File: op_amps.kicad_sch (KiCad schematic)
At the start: 44 parts, among them U10 ${SIM.PARAMS}, U11 ${SIM.PARAMS}, U12 ${SIM.PARAMS}, U13 ${SIM.PARAMS}, U14 ${SIM.PARAMS}, U15 ${SIM.PARAMS}, U16 ${SIM.PARAMS}, U17 ${SIM.PARAMS}, U18 ${SIM.PARAMS}, U19 ${SIM.PARAMS}, U20 ${SIM.PARAMS}, U21 ${SIM.PARAMS}, U22 ${SIM.PARAMS}, U23 ${SIM.PARAMS}, U8 ${SIM.PARAMS}, U9 ${SIM.PARAMS}

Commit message: Updated: crossbar
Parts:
- C1, C2, C3, C4: footprint Capacitor_SMD:C_1206_3216Metric_Pad1.33x1.80mm_HandSolder -> Capacitor_SMD:C_1206_3216Metric
- R15, R16, R17, R18, R19, R20, R21, R22, R23, R24, R25, R26, R27, R28, R29, R30, R31, R32, R33, R34, R44, R45, R46, R47: footprint Resistor_SMD:R_1206_3216Metric_Pad1.30x1.75mm_HandSolder -> Resistor_SMD:R_1206_3216Metric
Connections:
- net VCC renamed VDD

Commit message: Updated: crossbar error
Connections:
- net z1*: no longer R22.1, R27.1, R32.1, U12.4 (-), U16.4 (-), U20.4 (-)
- new net z2*: R22.1, U12.4 (-)
- new net z3*: R27.1, U16.4 (-)
- new net z4*: R32.1, U20.4 (-)
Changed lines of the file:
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@@
 		)
 	)
-	(global_label "z1*"
+	(global_label "z2*"
 		(shape input)
 		(at 43.18 100.33 180)
@@
 		)
 	)
-	(global_label "z1*"
+	(global_label "z3*"
 		(shape input)
 		(at 43.18 148.59 180)
@@
 		)
 	)
-	(global_label "z1*"
+	(global_label "z4*"
 		(shape input)
 		(at 43.18 195.58 180)

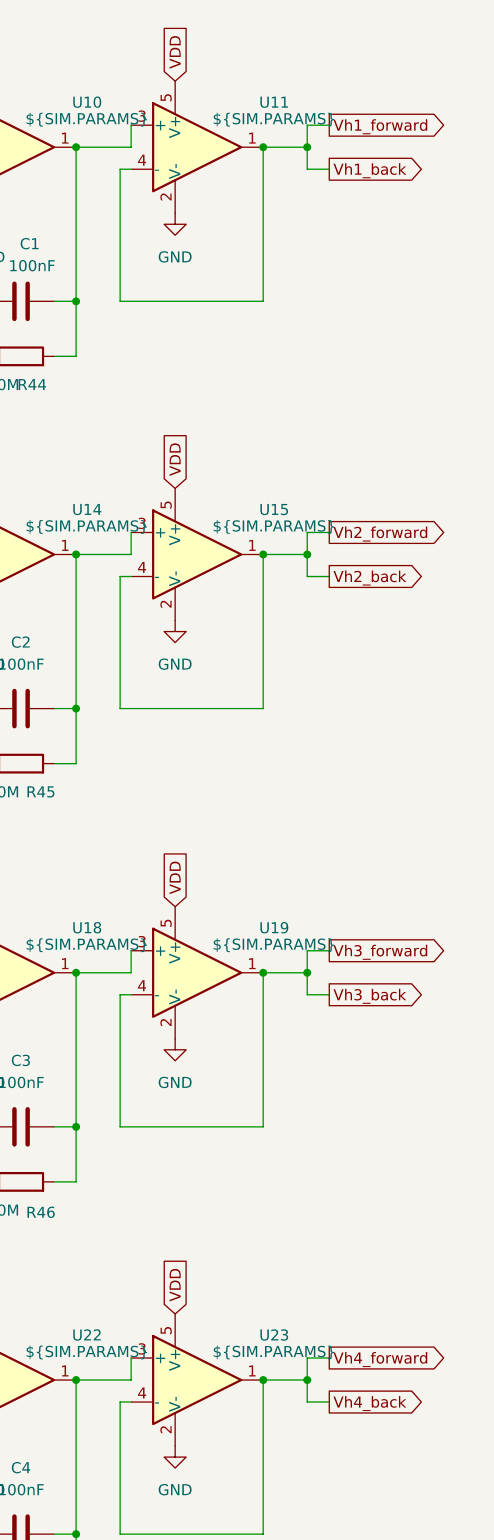
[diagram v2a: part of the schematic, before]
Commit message: Fixed: v closed loop
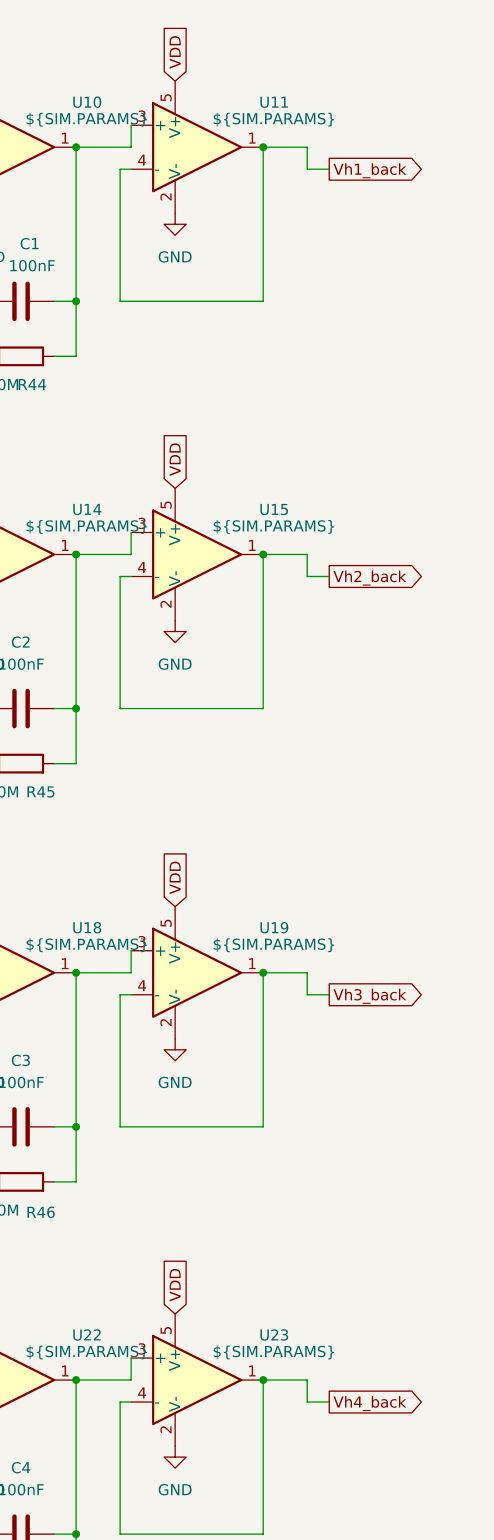
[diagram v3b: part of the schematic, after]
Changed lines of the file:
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@@
 	(paper "A4" portrait)
 	(junction
-		(at 153.67 148.59)
-		(diameter 0)
-		(color 0 0 0 0)
-	)
-	(junction
 		(at 127 166.37)
 		(diameter 0)
@@
 	)
 	(junction
-		(at 153.67 100.33)
-		(diameter 0)
-		(color 0 0 0 0)
-	)
-	(junction
 		(at 97.79 53.34)
 		(diameter 0)
@@
 	)
 	(junction
-		(at 153.67 53.34)
-		(diameter 0)
-		(color 0 0 0 0)
-	)
-	(junction
 		(at 49.53 151.13)
 		(diameter 0)
@@
 	)
 	(junction
-		(at 153.67 195.58)
-		(diameter 0)
-		(color 0 0 0 0)
-	)
-	(junction
 		(at 127 100.33)
 		(diameter 0)
@@
 	(wire
 		(pts
-			(xy 153.67 50.8) (xy 156.21 50.8)
-		)
-		(stroke
-			(width 0)
-			(type default)
-		)
-	)
-	(wire
-		(pts
 			(xy 132.08 151.13) (xy 133.35 151.13)
 		)
@@
 	(wire
 		(pts
-			(xy 153.67 146.05) (xy 153.67 148.59)
-		)
-		(stroke
-			(width 0)
-			(type default)
-		)
-	)
-	(wire
-		(pts
 			(xy 132.08 198.12) (xy 132.08 213.36)
 		)
@@
 	(wire
 		(pts
-			(xy 153.67 193.04) (xy 156.21 193.04)
-		)
-		(stroke
-			(width 0)
-			(type default)
-		)
-	)
-	(wire
-		(pts
 			(xy 49.53 55.88) (xy 49.53 71.12)
 		)
@@
 	(wire
 		(pts
-			(xy 153.67 97.79) (xy 156.21 97.79)
-		)
-		(stroke
-			(width 0)
-			(type default)
-		)
-	)
-	(wire
-		(pts
 			(xy 148.59 148.59) (xy 153.67 148.59)
 		)
@@
 	(wire
 		(pts
-			(xy 153.67 50.8) (xy 153.67 53.34)
-		)
-		(stroke
-			(width 0)
-			(type default)
-		)
-	)
-	(wire
-		(pts
 			(xy 153.67 100.33) (xy 153.67 102.87)
 		)
@@
 	(wire
 		(pts
-			(xy 153.67 146.05) (xy 156.21 146.05)
-		)
-		(stroke
-			(width 0)
-			(type default)
-		)
-	)
-	(wire
-		(pts
 			(xy 148.59 71.12) (xy 132.08 71.12)
 		)
@@
 	(wire
 		(pts
-			(xy 153.67 97.79) (xy 153.67 100.33)
-		)
-		(stroke
-			(width 0)
-			(type default)
-		)
-	)
-	(wire
-		(pts
 			(xy 148.59 100.33) (xy 153.67 100.33)
 		)
@@
 		(pts
 			(xy 111.76 213.36) (xy 116.84 213.36)
-		)
-		(stroke
-			(width 0)
-			(type default)
-		)
-	)
-	(wire
-		(pts
-			(xy 153.67 193.04) (xy 153.67 195.58)
 		)
 		(stroke
@@
 		)
 	)
-	(global_label "Vh4_forward"
-		(shape output)
-		(at 156.21 193.04 0)
-		(fields_autoplaced yes)
-		(effects
-			(font
-				(size 1.27 1.27)
-			)
-			(justify left)
-		)
-		(property "Intersheetrefs" "${INTERSHEET_REFS}"
-			(at 170.6855 193.04 0)
-			(effects
-				(font
-					(size 1.27 1.27)
-				)
-				(justify left)
-				(hide yes)
-			)
-		)
-	)
 	(global_label "VREF"
 		(shape input)
@@
 		)
 	)
-	(global_label "Vh3_forward"
-		(shape output)
-		(at 156.21 146.05 0)
-		(fields_autoplaced yes)
-		(effects
-			(font
-				(size 1.27 1.27)
-			)
-			(justify left)
-		)
-		(property "Intersheetrefs" "${INTERSHEET_REFS}"
-			(at 170.6855 146.05 0)
-			(effects
-				(font
-					(size 1.27 1.27)
-				)
-				(justify left)
-				(hide yes)
-			)
-		)
-	)
 	(global_label "z4*"
 		(shape input)
@@
 				(hide yes)
 			)
-		)
-	)
-	(global_label "Vh2_forward"
-		(shape output)
-		(at 156.21 97.79 0)
-		(fields_autoplaced yes)
-		(effects
-			(font
-				(size 1.27 1.27)
-			)
-			(justify left)
-		)
-		(property "Intersheetrefs" "${INTERSHEET_REFS}"
-			(at 170.6855 97.79 0)
-			(effects
-				(font
-					(size 1.27 1.27)
-				)
-				(justify left)
-				(hide yes)
-			)
-		)
-	)
-	(global_label "Vh1_forward"
-		(shape output)
-		(at 156.21 50.8 0)
-		(fields_autoplaced yes)
-		(effects
-			(font
-				(size 1.27 1.27)
-			)
-			(justify left)
-		)
-		(property "Intersheetrefs" "${INTERSHEET_REFS}"
-			(at 170.6855 50.8 0)
-			(effects
-				(font
-					(size 1.27 1.27)
-				)
-				(justify left)
-				(hide yes)
-			)
